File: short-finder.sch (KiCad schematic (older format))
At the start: 38 parts

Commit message: added values, pop options for tweaking
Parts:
- added C? (x2): 10uF, symbol C
- added C? (x3): 1uF, symbol C
- added C? (x2): 20nF, symbol C
- added C?: DNP, symbol C
- added R?: DNP, symbol R
- C?: value C -> 20nF
- C? (x2): value C -> 100pF
- C?: value C -> 10uF
- C?: value C -> 390pF
- C?: value C -> 470nF
- C?: value C -> 300pF
- C?: value C -> 1uF
- R? (x4): value R -> 100kR
- R?: value R -> 1MR
- R?: value R -> 10kR
- R?: value R -> 240kR
- R?: value R -> 6.81kR
- R?: renamed from RV?; value POT -> 1.5kR
- R?: value R -> 100R
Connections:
- wire segments 171 -> 196
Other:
- moved on the sheet: C?, Q?, R?, U?

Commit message: found a pot, value tweaks
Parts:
- removed J? (x2): CONN_01X01, symbol CONN_01X01
- added H? (x4): HOLE, symbol HOLE
- added J?: CONN_01X02, symbol CONN_01X02
- R?: value 6.81kR -> 6.8kR
- R?: value 1.5kR -> 1kR
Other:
- note added: "PVZ3A102C01R00"
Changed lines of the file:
@@
 P 1700 2950
 F 0 "R?" V 1780 2950 50  0000 C CNN
-F 1 "6.81kR" V 1707 2951 50  0000 C CNN
+F 1 "6.8kR" V 1707 2951 50  0000 C CNN
 F 2 "" V 1630 2950 30  0000 C CNN
 F 3 "" H 1700 2950 30  0000 C CNN
@@
 P 1700 3650
 F 0 "R?" H 1700 3550 50  0000 C CNN
-F 1 "1.5kR" H 1700 3650 50  0000 C CNN
+F 1 "1kR" H 1700 3650 50  0000 C CNN
 F 2 "" H 1700 3650 60  0000 C CNN
 F 3 "" H 1700 3650 60  0000 C CNN
@@
 F 3 "" H 8100 3900 60  0000 C CNN
 	1    8100 3900
-	1    0    0    -1
-$EndComp
-$Comp
-L CONN_01X01 J?
-U 1 1 54D74111
-P 11600 6200
-F 0 "J?" H 11600 6300 50  0000 C CNN
-F 1 "CONN_01X01" H 11950 6200 50  0000 C CNN
-F 2 "" H 11600 6200 60  0000 C CNN
-F 3 "" H 11600 6200 60  0000 C CNN
-	1    11600 6200
-	1    0    0    -1
-$EndComp
-$Comp
-L CONN_01X01 J?
-U 1 1 54D74423
-P 11600 6400
-F 0 "J?" H 11600 6500 50  0000 C CNN
-F 1 "CONN_01X01" H 11950 6400 50  0000 C CNN
-F 2 "" H 11600 6400 60  0000 C CNN
-F 3 "" H 11600 6400 60  0000 C CNN
-	1    11600 6400
 	1    0    0    -1
 $EndComp
@@
 L GND #PWR?
 U 1 1 54D86EF5
-P 11300 6500
-F 0 "#PWR?" H 11300 6250 60  0001 C CNN
-F 1 "GND" H 11300 6350 60  0000 C CNN
-F 2 "" H 11300 6500 60  0000 C CNN
-F 3 "" H 11300 6500 60  0000 C CNN
-	1    11300 6500
-	1    0    0    -1
-$EndComp
-Wire Wire Line
-	11300 6400 11300 6500
-Wire Wire Line
-	11400 6400 11300 6400
+P 11300 6400
+F 0 "#PWR?" H 11300 6150 60  0001 C CNN
+F 1 "GND" H 11300 6250 60  0000 C CNN
+F 2 "" H 11300 6400 60  0000 C CNN
+F 3 "" H 11300 6400 60  0000 C CNN
+	1    11300 6400
+	1    0    0    -1
+$EndComp
+Wire Wire Line
+	11300 6300 11300 6400
+Wire Wire Line
+	11400 6300 11300 6300
 $Comp
 L GND #PWR?
@@
 L GND #PWR?
 U 1 1 54D8F9CD
-P 8400 6750
-F 0 "#PWR?" H 8400 6500 60  0001 C CNN
-F 1 "GND" H 8400 6600 60  0000 C CNN
-F 2 "" H 8400 6750 60  0000 C CNN
-F 3 "" H 8400 6750 60  0000 C CNN
-	1    8400 6750
-	1    0    0    -1
-$EndComp
-Wire Wire Line
-	8400 6650 8400 6750
+P 8400 6800
+F 0 "#PWR?" H 8400 6550 60  0001 C CNN
+F 1 "GND" H 8400 6650 60  0000 C CNN
+F 2 "" H 8400 6800 60  0000 C CNN
+F 3 "" H 8400 6800 60  0000 C CNN
+	1    8400 6800
+	1    0    0    -1
+$EndComp
+Wire Wire Line
+	8400 6700 8400 6800
 $Comp
 L CONN_01X02 J?
@@
 	1300 3300 1700 3300
 Connection ~ 1700 3300
+$Comp
+L HOLE H?
+U 1 1 54DB196B
+P 14900 1900
+F 0 "H?" H 14900 2050 60  0000 C CNN
+F 1 "HOLE" H 14900 1750 60  0000 C CNN
+F 2 "" H 14900 1900 60  0000 C CNN
+F 3 "" H 14900 1900 60  0000 C CNN
+	1    14900 1900
+	1    0    0    -1
+$EndComp
+$Comp
+L HOLE H?
+U 1 1 54DB1BDC
+P 14900 2400
+F 0 "H?" H 14900 2550 60  0000 C CNN
+F 1 "HOLE" H 14900 2250 60  0000 C CNN
+F 2 "" H 14900 2400 60  0000 C CNN
+F 3 "" H 14900 2400 60  0000 C CNN
+	1    14900 2400
+	1    0    0    -1
+$EndComp
+$Comp
+L HOLE H?
+U 1 1 54DB1DB5
+P 14900 2900
+F 0 "H?" H 14900 3050 60  0000 C CNN
+F 1 "HOLE" H 14900 2750 60  0000 C CNN
+F 2 "" H 14900 2900 60  0000 C CNN
+F 3 "" H 14900 2900 60  0000 C CNN
+	1    14900 2900
+	1    0    0    -1
+$EndComp
+$Comp
+L HOLE H?
+U 1 1 54DB1DBB
+P 14900 3400
+F 0 "H?" H 14900 3550 60  0000 C CNN
+F 1 "HOLE" H 14900 3250 60  0000 C CNN
+F 2 "" H 14900 3400 60  0000 C CNN
+F 3 "" H 14900 3400 60  0000 C CNN
+	1    14900 3400
+	1    0    0    -1
+$EndComp
+$Comp
+L CONN_01X02 J?
+U 1 1 54DB23DF
+P 11600 6250
+F 0 "J?" H 11600 6400 50  0000 C CNN
+F 1 "CONN_01X02" V 11700 6250 50  0000 C CNN
+F 2 "" H 11600 6250 60  0000 C CNN
+F 3 "" H 11600 6250 60  0000 C CNN
+	1    11600 6250
+	1    0    0    -1
+$EndComp
+Text Notes 1300 4350 0    60   ~ 0
+PVZ3A102C01R00
 $EndSCHEMATC

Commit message: annotated
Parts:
- gave numbers to parts that had none: 50

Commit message: netlist
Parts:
- C1, C10, C11, C12, C13, C14, C15, C2, C3, C4, C5, C6, C7, C8, C9: footprint (none) -> !Parts:SMD-0402-C
- C16: footprint (none) -> SMD_Packages:SMD-0805
- H1, H2, H3, H4: footprint (none) -> !Parts:M2-HOLE
- J1: footprint (none) -> !Parts:MICRO-USB-10104111
- J2: footprint (none) -> Pin_Headers:Pin_Header_Straight_2x03
- J3: footprint (none) -> !Parts:POMONA_6883
- J4, J5, J6, J7, J8: footprint (none) -> Pin_Headers:Pin_Header_Straight_1x02
- P1: footprint (none) -> Pin_Headers:Pin_Header_Straight_1x03
- Q1, Q2, Q3, Q4: footprint SOT-23 -> SMD_Packages:SOT-23
- R1, R10, R11, R2, R4, R5, R6, R7, R8, R9: footprint (none) -> !Parts:SMD-0402-R
- R3: footprint (none) -> !Parts:PVZ3A
- U1, U2: footprint (none) -> Housings_SOIC:SOIC-8_3.9x4.9mm_Pitch1.27mm
- U3: footprint (none) -> Housings_SOIC:SOIC-16_3.9x9.9mm_Pitch1.27mm
- U4: footprint (none) -> Housings_SOIC:SOIC-14_3.9x8.7mm_Pitch1.27mm
- U5: footprint (none) -> Housings_SOT-23_SOT-143_TSOT-6:SC70-6
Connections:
- wire segments 196 -> 157

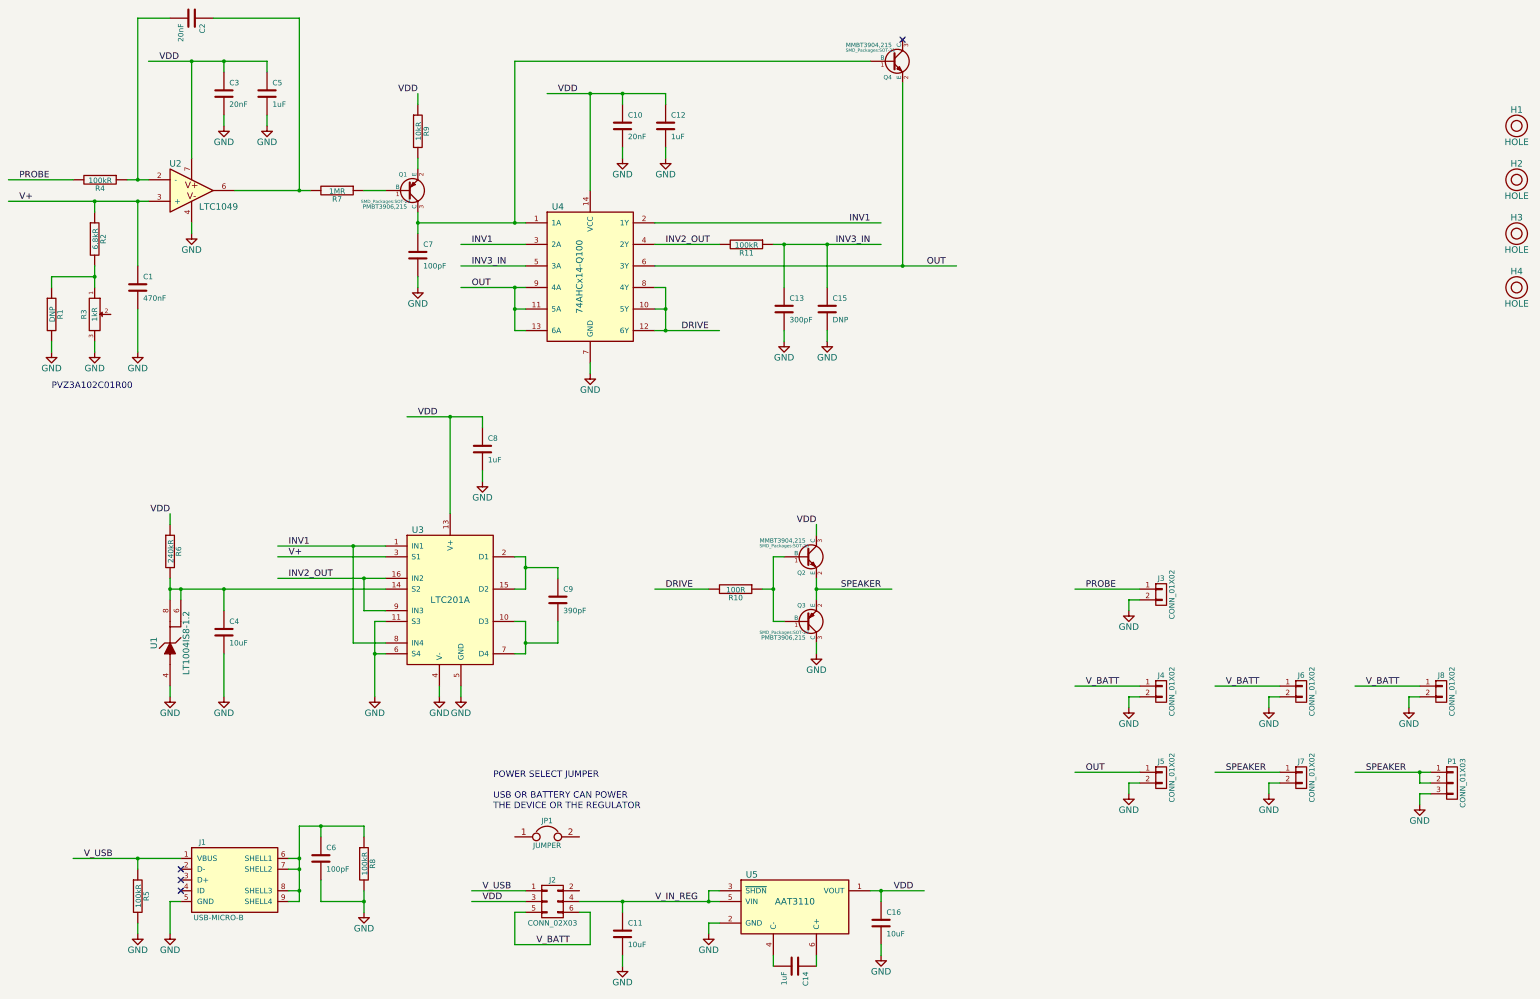
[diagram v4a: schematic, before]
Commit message: named (all?) remaining nets
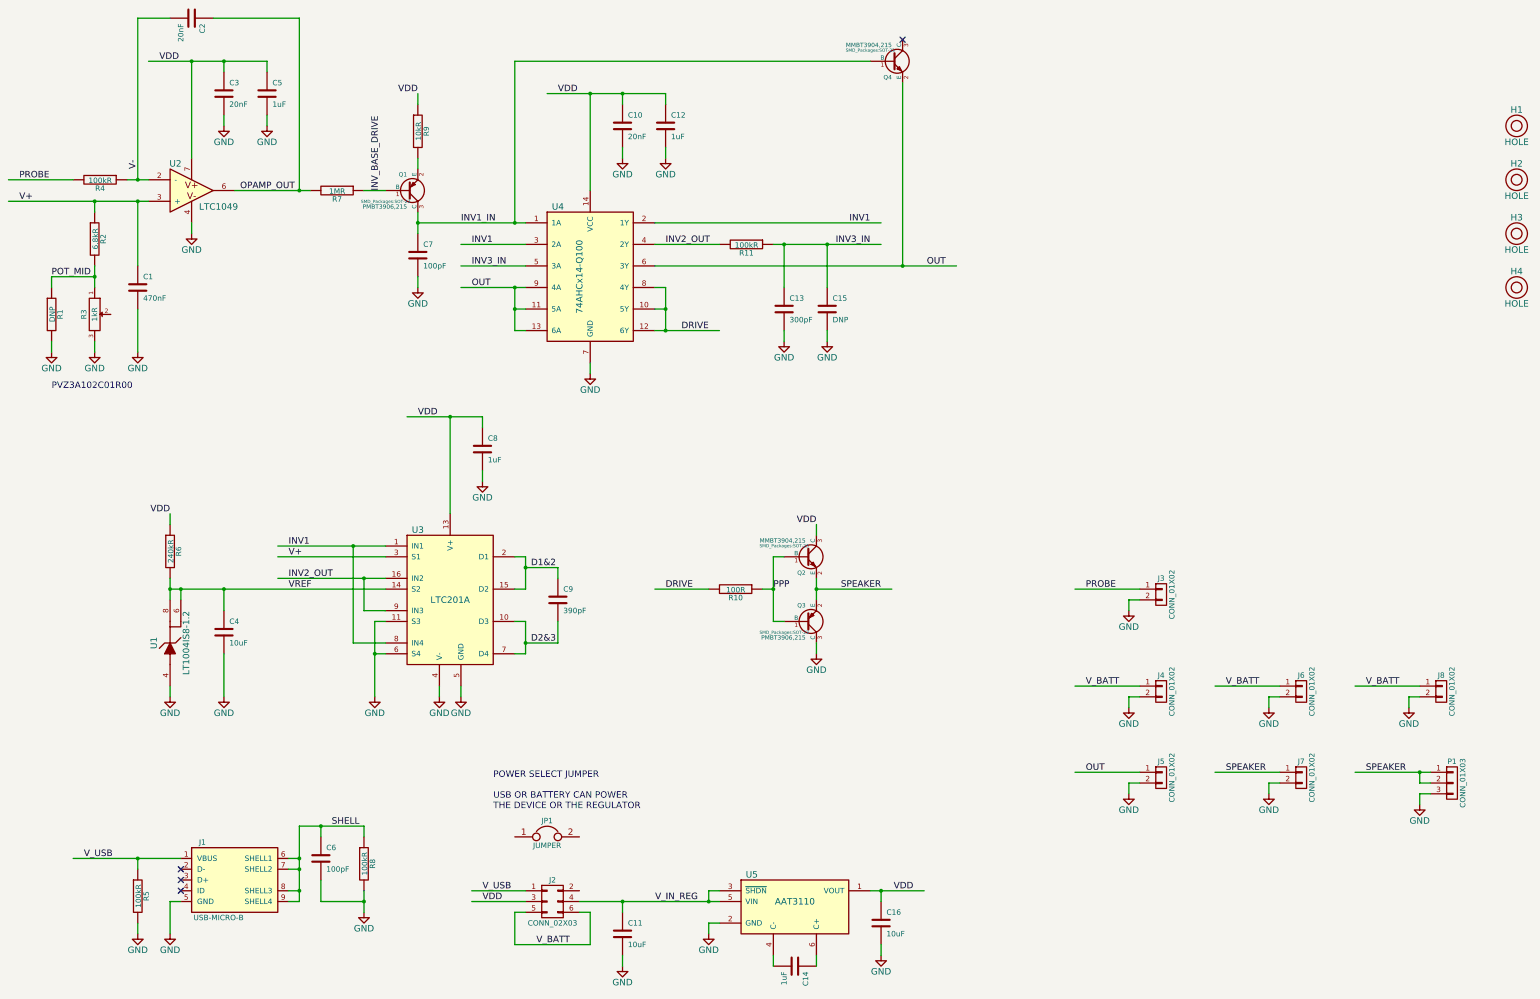
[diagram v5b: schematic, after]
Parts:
- U5: footprint Housings_SOT-23_SOT-143_TSOT-6:SC70-6 -> SMD_Packages:SOT-23-6
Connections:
- net labels added: D1&2, D2&3, INV1_IN, INV_BASE_DRIVE, OPAMP_OUT, POT_MID, PPP, SHELL, V-, VREF
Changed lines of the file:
@@
 F 0 "U5" H 7800 9350 60  0000 C CNN
 F 1 "AAT3110" H 8200 9100 60  0000 C CNN
-F 2 "Housings_SOT-23_SOT-143_TSOT-6:SC70-6" H 8200 9100 60  0001 C CNN
+F 2 "SMD_Packages:SOT-23-6" H 8200 9100 60  0001 C CNN
 F 3 "" H 8200 9100 60  0000 C CNN
 	1    8200 9100
@@
 Text Notes 1300 4350 0    60   ~ 0
 PVZ3A102C01R00
+Text Label 8000 6200 0    60   ~ 0
+PPP
+Text Label 5750 6000 0    60   ~ 0
+D1&2
+Text Label 5750 6700 0    60   ~ 0
+D2&3
+Text Label 3900 8400 0    60   ~ 0
+SHELL
+Text Label 1300 3300 0    60   ~ 0
+POT_MID
+Text Label 3050 2500 0    60   ~ 0
+OPAMP_OUT
+Text Label 2100 2300 1    60   ~ 0
+V-
+Text Label 5100 2800 0    60   ~ 0
+INV1_IN
+Text Label 4350 2500 1    60   ~ 0
+INV_BASE_DRIVE
+Text Label 3500 6200 0    60   ~ 0
+VREF
 $EndSCHEMATC

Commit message: reannotated slightly and started to think about placement
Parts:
- renumbered P1 to J9
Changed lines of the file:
@@
 SPEAKER
 $Comp
-L CONN_01X03 P1
+L CONN_01X03 J9
 U 1 1 54D92F5A
 P 14300 8000
-F 0 "P1" H 14300 8200 50  0000 C CNN
+F 0 "J9" H 14300 8200 50  0000 C CNN
 F 1 "CONN_01X03" V 14400 8000 50  0000 C CNN
 F 2 "Pin_Headers:Pin_Header_Straight_1x03" H 14300 8000 60  0001 C CNN
